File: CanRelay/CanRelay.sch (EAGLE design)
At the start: 21 parts

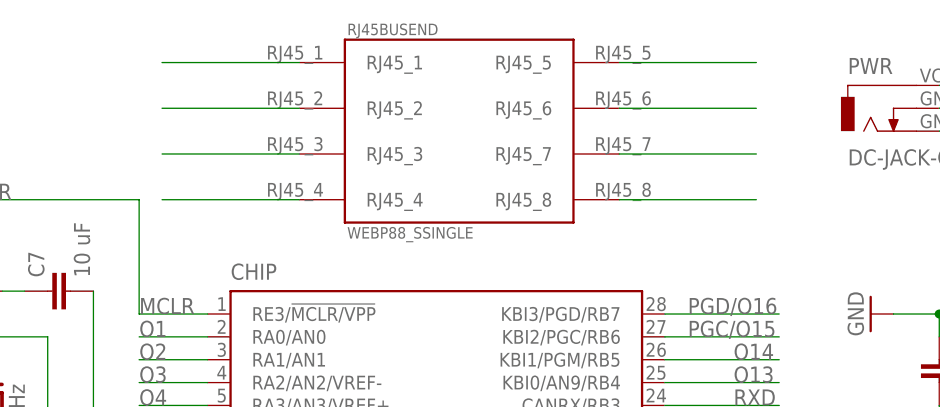
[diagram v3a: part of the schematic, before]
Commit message: #10 adding more missing GND vias to the board, running checks, adding  missing labels in schematic, done  #
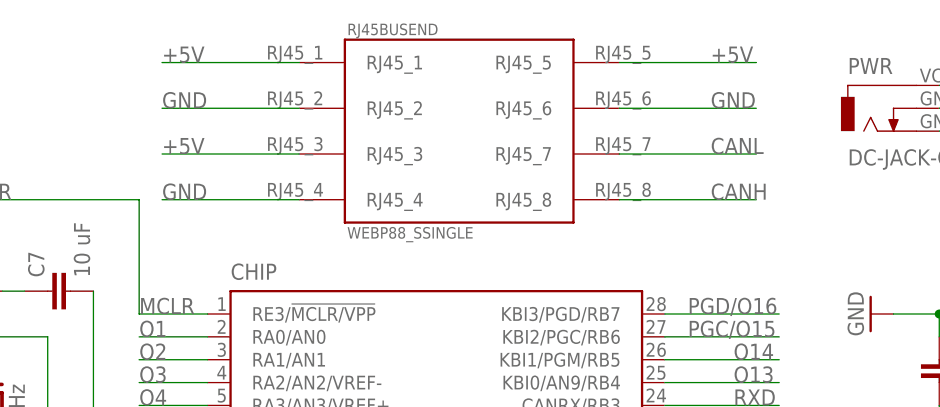
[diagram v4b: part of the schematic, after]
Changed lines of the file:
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@@
 <pinref part="RJ45BUSEND" gate="G$1" pin="RJ45_1"/>
 <wire x1="-91.44" y1="132.08" x2="-106.68" y2="132.08" width="0.1524" layer="91"/>
+<label x="-106.68" y="132.08" size="1.778" layer="95"/>
 </segment>
 <segment>
 <pinref part="RJ45BUSEND" gate="G$1" pin="RJ45_3"/>
 <wire x1="-91.44" y1="121.92" x2="-106.68" y2="121.92" width="0.1524" layer="91"/>
+<label x="-106.68" y="121.92" size="1.778" layer="95"/>
 </segment>
 <segment>
 <pinref part="RJ45BUSEND" gate="G$1" pin="RJ45_5"/>
 <wire x1="-55.88" y1="132.08" x2="-40.64" y2="132.08" width="0.1524" layer="91"/>
+<label x="-45.72" y="132.08" size="1.778" layer="95"/>
 </segment>
 </net>
@@
 <pinref part="RJ45BUSEND" gate="G$1" pin="RJ45_2"/>
 <wire x1="-91.44" y1="127" x2="-106.68" y2="127" width="0.1524" layer="91"/>
+<label x="-106.68" y="127" size="1.778" layer="95"/>
 </segment>
 <segment>
 <pinref part="RJ45BUSEND" gate="G$1" pin="RJ45_4"/>
 <wire x1="-91.44" y1="116.84" x2="-106.68" y2="116.84" width="0.1524" layer="91"/>
+<label x="-106.68" y="116.84" size="1.778" layer="95"/>
 </segment>
 <segment>
 <pinref part="RJ45BUSEND" gate="G$1" pin="RJ45_6"/>
 <wire x1="-55.88" y1="127" x2="-40.64" y2="127" width="0.1524" layer="91"/>
+<label x="-45.72" y="127" size="1.778" layer="95"/>
 </segment>
 </net>
@@
 <pinref part="RJ45BUSEND" gate="G$1" pin="RJ45_8"/>
 <wire x1="-55.88" y1="116.84" x2="-40.64" y2="116.84" width="0.1524" layer="91"/>
+<label x="-45.72" y="116.84" size="1.778" layer="95"/>
 </segment>
 </net>
@@
 <pinref part="RJ45BUSEND" gate="G$1" pin="RJ45_7"/>
 <wire x1="-55.88" y1="121.92" x2="-40.64" y2="121.92" width="0.1524" layer="91"/>
-</segment>
-</net>
+<label x="-45.72" y="121.92" size="1.778" layer="95"/>
+</segment>
+</net>

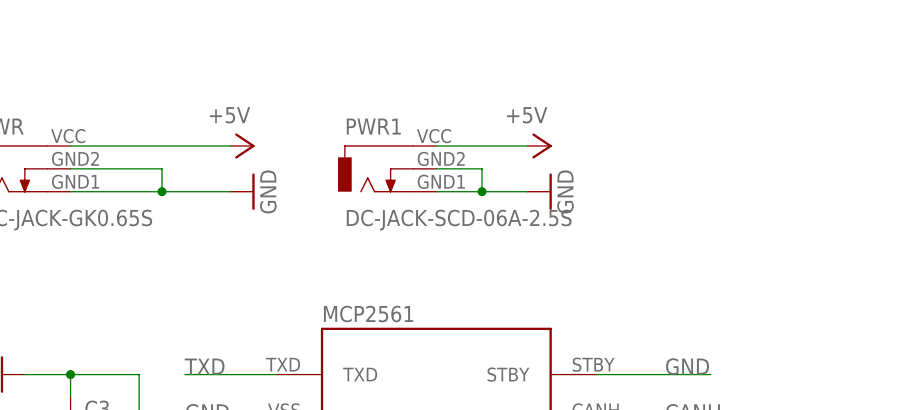
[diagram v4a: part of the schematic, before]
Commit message: #16 adding new FUSE component  - created before a new simple component from GME and added to schema  now  - wired up all, created new signal, used VCC for name and label +5V-RAW  - this is the actual power from the adapter, but FUSE would translate  that to +5V that all pins on the board use and need  - more tweaks and edits to make it all on the board  - labels and vias shuffled around too  - need to check the actual size of transceiver to make sure it can all  fit the board
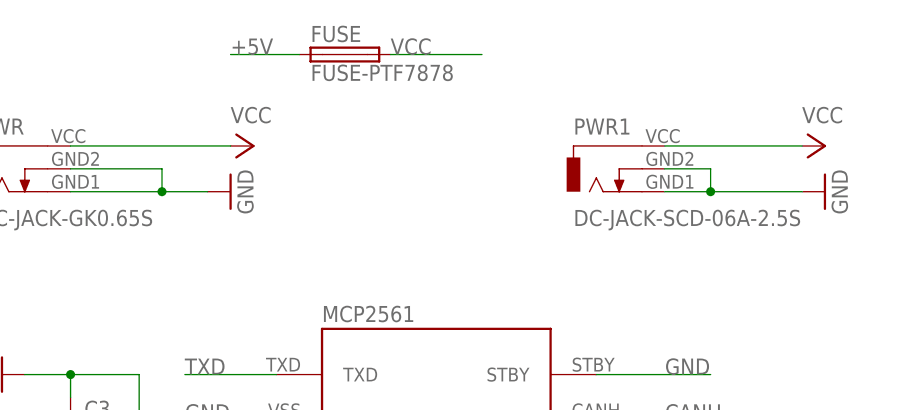
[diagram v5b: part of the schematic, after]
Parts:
- added FUSE: FUSE-PTF7878, PoJD:FUSE-PTF7878
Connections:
- new net VCC: FUSE.2, PWR.VCC, PWR1.VCC
- net +5V: now also FUSE.1; no longer PWR.VCC, PWR1.VCC
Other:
- moved on the sheet: PWR1
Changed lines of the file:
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@@
 <part name="PWR" library="PoJD" deviceset="DC-JACK-GK0.65" device="S"/>
 <part name="GND9" library="supply1" deviceset="GND" device=""/>
-<part name="P+5" library="supply1" deviceset="+5V" device=""/>
 <part name="USBTIN" library="pinhead" deviceset="PINHD-1X3" device=""/>
-<part name="P+6" library="supply1" deviceset="+5V" device=""/>
 <part name="GND10" library="supply1" deviceset="GND" device=""/>
 <part name="PWR1" library="PoJD" deviceset="DC-JACK-SCD-06A-2.5" device="S"/>
+<part name="FUSE" library="PoJD" deviceset="FUSE-PTF78" device="78"/>
+<part name="P+4" library="supply1" deviceset="VCC" device=""/>
+<part name="P+5" library="supply1" deviceset="VCC" device=""/>
 </parts>
 <sheets>
@@
 <instance part="RJ45BUSEND" gate="G$1" x="-73.66" y="124.46"/>
 <instance part="PWR" gate="G$1" x="-27.94" y="127"/>
-<instance part="GND9" gate="1" x="0" y="124.46" rot="R90"/>
-<instance part="P+5" gate="1" x="0" y="129.54" rot="R270"/>
+<instance part="GND9" gate="1" x="-2.54" y="124.46" rot="R90"/>
 <instance part="USBTIN" gate="A" x="7.62" y="50.8"/>
-<instance part="P+6" gate="1" x="33.02" y="129.54" rot="R270"/>
-<instance part="GND10" gate="1" x="33.02" y="124.46" rot="R90"/>
-<instance part="PWR1" gate="G$1" x="12.7" y="127"/>
+<instance part="GND10" gate="1" x="63.5" y="124.46" rot="R90"/>
+<instance part="PWR1" gate="G$1" x="38.1" y="127"/>
+<instance part="FUSE" gate="G$1" x="10.16" y="139.7"/>
+<instance part="P+4" gate="VCC" x="0" y="129.54" rot="R270"/>
+<instance part="P+5" gate="VCC" x="63.5" y="129.54" rot="R270"/>
 </instances>
 <busses>
@@
 </segment>
 <segment>
-<pinref part="PWR" gate="G$1" pin="VCC"/>
-<pinref part="P+5" gate="1" pin="+5V"/>
-<wire x1="-20.32" y1="129.54" x2="-2.54" y2="129.54" width="0.1524" layer="91"/>
-</segment>
-<segment>
-<pinref part="PWR1" gate="G$1" pin="VCC"/>
-<pinref part="P+6" gate="1" pin="+5V"/>
-<wire x1="20.32" y1="129.54" x2="30.48" y2="129.54" width="0.1524" layer="91"/>
-</segment>
-<segment>
 <pinref part="RJ45BUSEND" gate="G$1" pin="RJ45_1"/>
 <wire x1="-91.44" y1="132.08" x2="-106.68" y2="132.08" width="0.1524" layer="91"/>
@@
 <wire x1="-55.88" y1="132.08" x2="-40.64" y2="132.08" width="0.1524" layer="91"/>
 <label x="-45.72" y="132.08" size="1.778" layer="95"/>
+</segment>
+<segment>
+<pinref part="FUSE" gate="G$1" pin="1"/>
+<wire x1="5.08" y1="139.7" x2="-2.54" y2="139.7" width="0.1524" layer="91"/>
+<label x="-2.54" y="139.7" size="1.778" layer="95"/>
 </segment>
 </net>
@@
 <wire x1="-20.32" y1="124.46" x2="-10.16" y2="124.46" width="0.1524" layer="91"/>
 <pinref part="PWR" gate="G$1" pin="GND2"/>
-<wire x1="-10.16" y1="124.46" x2="-2.54" y2="124.46" width="0.1524" layer="91"/>
+<wire x1="-10.16" y1="124.46" x2="-5.08" y2="124.46" width="0.1524" layer="91"/>
 <wire x1="-20.32" y1="127" x2="-10.16" y2="127" width="0.1524" layer="91"/>
 <wire x1="-10.16" y1="127" x2="-10.16" y2="124.46" width="0.1524" layer="91"/>
@@
 <segment>
 <pinref part="PWR1" gate="G$1" pin="GND2"/>
-<wire x1="20.32" y1="127" x2="25.4" y2="127" width="0.1524" layer="91"/>
-<wire x1="25.4" y1="127" x2="25.4" y2="124.46" width="0.1524" layer="91"/>
+<wire x1="45.72" y1="127" x2="50.8" y2="127" width="0.1524" layer="91"/>
+<wire x1="50.8" y1="127" x2="50.8" y2="124.46" width="0.1524" layer="91"/>
 <pinref part="PWR1" gate="G$1" pin="GND1"/>
-<wire x1="20.32" y1="124.46" x2="25.4" y2="124.46" width="0.1524" layer="91"/>
+<wire x1="45.72" y1="124.46" x2="50.8" y2="124.46" width="0.1524" layer="91"/>
 <pinref part="GND10" gate="1" pin="GND"/>
-<wire x1="25.4" y1="124.46" x2="30.48" y2="124.46" width="0.1524" layer="91"/>
-<junction x="25.4" y="124.46"/>
+<wire x1="50.8" y1="124.46" x2="60.96" y2="124.46" width="0.1524" layer="91"/>
+<junction x="50.8" y="124.46"/>
 </segment>
 <segment>
@@
 </segment>
 </net>
+<net name="VCC" class="0">
+<segment>
+<pinref part="PWR" gate="G$1" pin="VCC"/>
+<pinref part="P+4" gate="VCC" pin="VCC"/>
+<wire x1="-20.32" y1="129.54" x2="-2.54" y2="129.54" width="0.1524" layer="91"/>
+</segment>
+<segment>
+<pinref part="PWR1" gate="G$1" pin="VCC"/>
+<pinref part="P+5" gate="VCC" pin="VCC"/>
+<wire x1="45.72" y1="129.54" x2="60.96" y2="129.54" width="0.1524" layer="91"/>
+</segment>
+<segment>
+<pinref part="FUSE" gate="G$1" pin="2"/>
+<wire x1="15.24" y1="139.7" x2="25.4" y2="139.7" width="0.1524" layer="91"/>
+<label x="15.24" y="139.7" size="1.778" layer="95"/>
+</segment>
+</net>
